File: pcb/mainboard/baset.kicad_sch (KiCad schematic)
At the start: 47 parts, among them U38 ISL24021IRT065Z-T7A‎, U39 ISL24021IRT065Z-T7A‎, U40 ISL24021IRT065Z-T7A‎, U41 ISL24021IRT065Z-T7A‎, U42 DACx0508_WQFN, U43 ISL24021IRT065Z-T7A‎, U44 ISL24021IRT065Z-T7A‎, U45 ISL24021IRT065Z-T7A‎, U46 ISL24021IRT065Z-T7A‎, U8 XC7K70T-2FBG484C

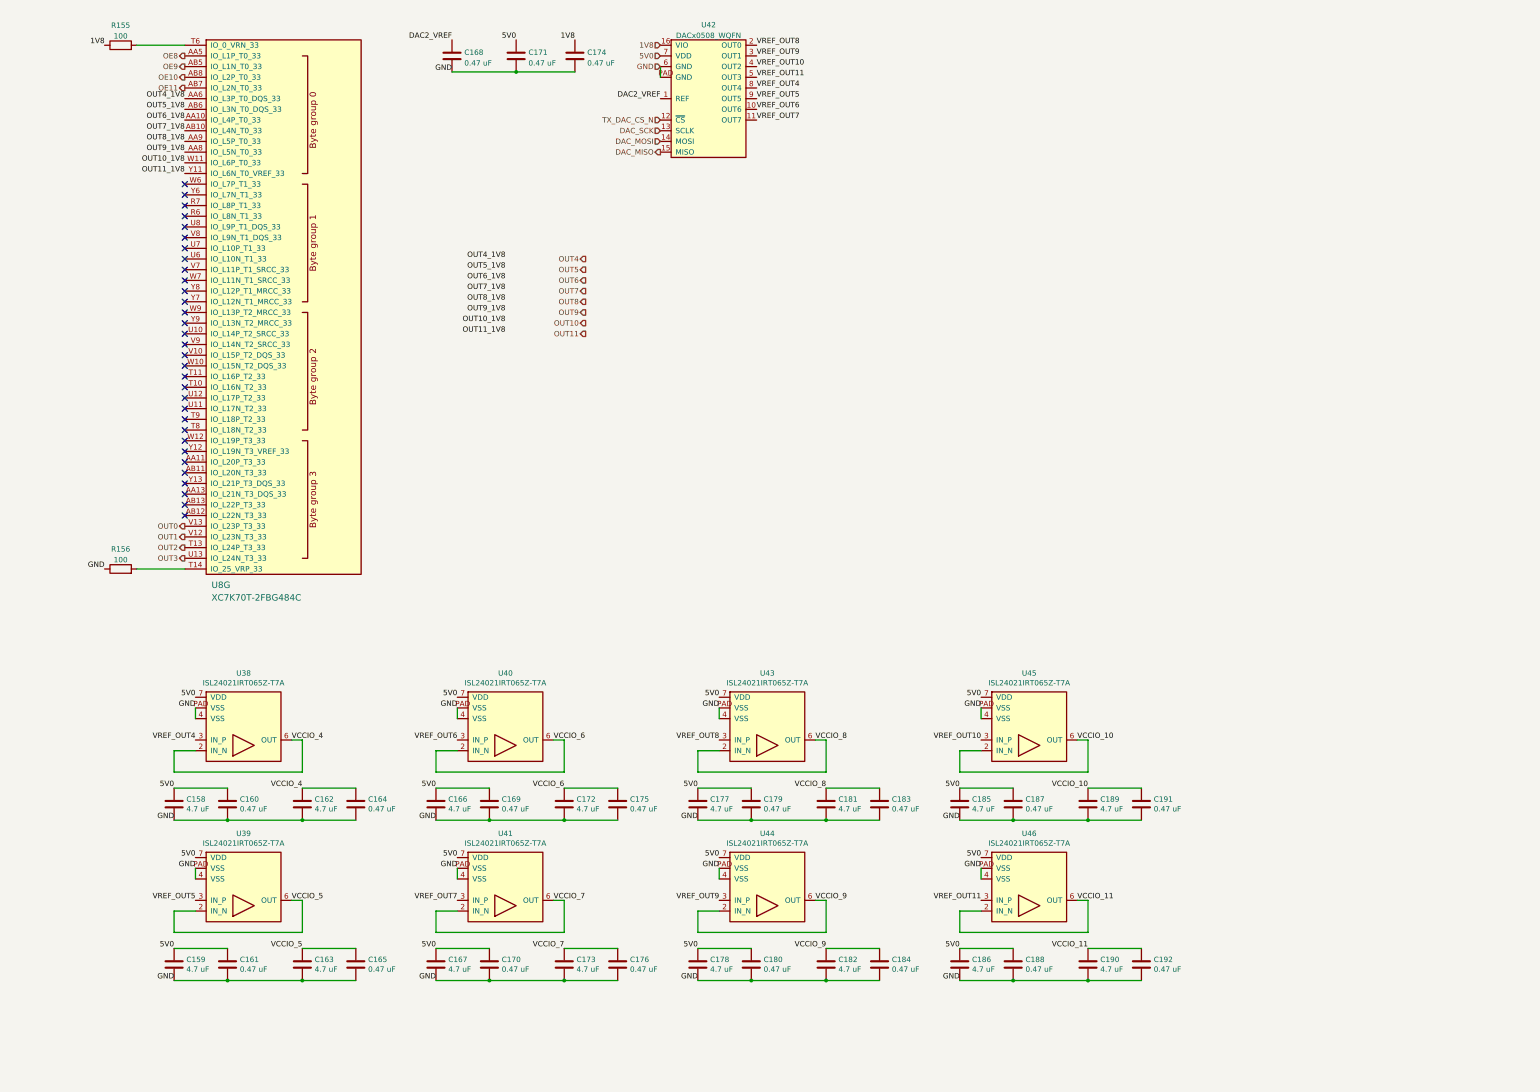
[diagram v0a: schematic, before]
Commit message: Continued initial work on main board
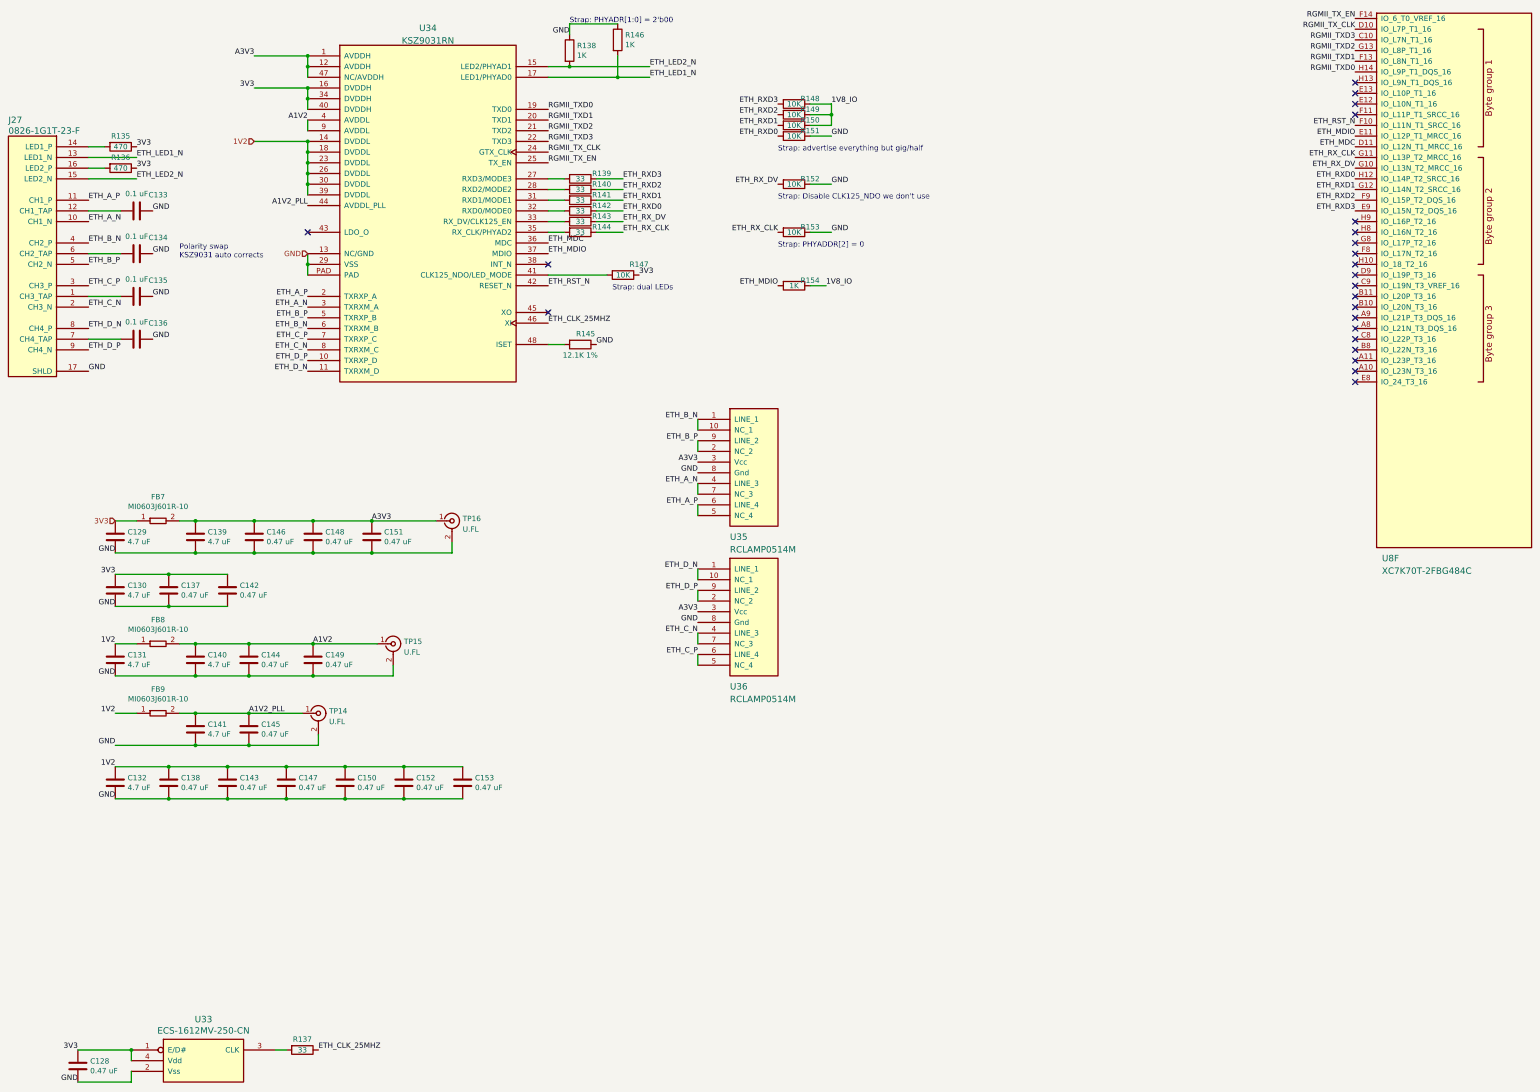
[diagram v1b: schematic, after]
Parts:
- removed C158, C159, C162, C163, C166, C167, C172, C173, C177, C178, C181, C182, C185, C186, C189, C190: 4.7 uF, azonenberg_pcb:EIA_0603_CAP_NOSILK, symbol device:C
- removed C160, C161, C164, C165, C169, C170, C175, C176, C179, C180, C183, C184, C187, C188, C191, C192: 0.47 uF, azonenberg_pcb:EIA_0402_CAP_NOSILK, symbol device:C
- removed C168, C171, C174: 0.47 uF, symbol device:C
- removed R155, R156: 100, symbol device:R
- removed U38, U39, U40, U41, U43, U44, U45, U46: ISL24021IRT065Z-T7A‎, azonenberg_pcb:DFN_8_0.65MM_3x3MM, symbol analog-azonenberg:ISL24021IRT065Z-T7A‎
- removed U42: DACx0508_WQFN, symbol analog-azonenberg:DACx0508_WQFN
- removed U8: XC7K70T-2FBG484C, symbol xilinx-azonenberg:XC7KxT-FBG484
- added C128, C137, C138, C142, C143, C144, C145, C146, C147, C148, C149, C150, C151, C152, C153: 0.47 uF, symbol device:C
- added C129, C130, C131, C132, C139, C140, C141: 4.7 uF, symbol device:C
- added C133, C134, C135, C136: 0.1 uF, symbol device:C
- added FB7, FB8, FB9: MI0603J601R-10, symbol passive-azonenberg:FERRITE_SMALL2
- added J27: 0826-1G1T-23-F, symbol special-azonenberg:BEL_FUSE_0826-1G1T-23-F
- added R135, R136: 470, symbol device:R
- added R137, R139, R140, R141, R142, R143, R144: 33, symbol device:R
- added R138, R146, R154: 1K, symbol device:R
- added R145: 12.1K 1%, symbol device:R
- added R147, R148, R149, R150, R151, R152, R153: 10K, symbol device:R
- added TP14, TP15, TP16: U.FL, symbol conn:CONN_COAXIAL
- added U33: ECS-1612MV-250-CN, symbol osc-azonenberg:OSC
- added U34: KSZ9031RN, symbol special-azonenberg:KSZ9031RN
- added U35, U36: RCLAMP0514M, symbol special-azonenberg:RCLAMP0514M
- added U8: XC7K70T-2FBG484C, symbol xilinx-azonenberg:XC7KxT-FBG484
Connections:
- net GND: now also C128.2, C129.2, C130.2, C131.2, C132.2, C133.1, C134.1, C135.1, C136.1, C137.2, C138.2, C139.2, C140.2, C141.2, C142.2, C143.2, C144.2, C145.2, C146.2, C147.2, C148.2, C149.2, C150.2, C151.2, C152.2, C153.2, J27.17 (SHLD), R138.1, R145.1, R146.1, R151.1, R152.1, R153.1, TP14.2 (Ext), TP15.2 (Ext), TP16.2 (Ext), U33.2 (Vss), U34.13 (NC/GND), U34.29 (VSS), U34.PAD, U35.8 (Gnd), U36.8 (Gnd)
- new net: R147.2, U34.41 (CLK125_NDO/LED_MODE)
- new net: R140.2, U34.28 (RXD2/MODE2)
- new net: R145.2, U34.48 (ISET)
- new net: C133.2, J27.12 (CH1_TAP)
- new net: R139.2, U34.27 (RXD3/MODE3)
- new net: C135.2, J27.1 (CH3_TAP)
- new net: J27.14 (LED1_P), R135.2
- new net: J27.16 (LED2_P), R136.2
- new net: C134.2, J27.6 (CH2_TAP)
- new net: C136.2, J27.7 (CH4_TAP)
- new net: R141.2, U34.31 (RXD1/MODE1)
- new net: R142.2, U34.32 (RXD0/MODE0)
- new net: R143.2, U34.33 (RX_DV/CLK125_EN)
- new net: R144.2, U34.35 (RX_CLK/PHYAD2)
- new net: R137.2, U33.3 (CLK)
- new net 1V2: C131.1, C132.1, C138.1, C143.1, C147.1, C150.1, C152.1, C153.1, FB8.1, FB9.1, U34.14 (DVDDL), U34.18 (DVDDL), U34.23 (DVDDL), U34.26 (DVDDL), U34.30 (DVDDL), U34.39 (DVDDL)
- new net 1V8_IO: R148.1, R149.1, R150.1, R154.1
- new net 3V3: C128.1, C129.1, C130.1, C137.1, C142.1, FB7.1, R135.1, R136.1, R147.1, U33.1 (E/D#), U33.4 (Vdd), U34.16 (DVDDH), U34.34 (DVDDH), U34.40 (DVDDH)
- new net A1V2: C140.1, C144.1, C149.1, FB8.2, TP15.1 (In), U34.4 (AVDDL), U34.9 (AVDDL)
- new net A1V2_PLL: C141.1, C145.1, FB9.2, TP14.1 (In), U34.44 (AVDDL_PLL)
- new net A3V3: C139.1, C146.1, C148.1, C151.1, FB7.2, TP16.1 (In), U34.1 (AVDDH), U34.12 (AVDDH), U34.47 (NC/AVDDH), U35.3 (Vcc), U36.3 (Vcc)
- new net ETH_A_N: J27.10 (CH1_N), U34.3 (TXRXM_A), U35.4 (LINE_3), U35.7 (NC_3)
- new net ETH_A_P: J27.11 (CH1_P), U34.2 (TXRXP_A), U35.5 (NC_4), U35.6 (LINE_4)
- new net ETH_B_N: J27.4 (CH2_P), U34.6 (TXRXM_B), U35.1 (LINE_1), U35.10 (NC_1)
- new net ETH_B_P: J27.5 (CH2_N), U34.5 (TXRXP_B), U35.2 (NC_2), U35.9 (LINE_2)
- new net ETH_CLK_25MHZ: R137.1, U34.46 (XI)
- new net ETH_C_N: J27.2 (CH3_N), U34.8 (TXRXM_C), U36.4 (LINE_3), U36.7 (NC_3)
- new net ETH_C_P: J27.3 (CH3_P), U34.7 (TXRXP_C), U36.5 (NC_4), U36.6 (LINE_4)
- new net ETH_D_N: J27.8 (CH4_P), U34.11 (TXRXM_D), U36.1 (LINE_1), U36.10 (NC_1)
- new net ETH_D_P: J27.9 (CH4_N), U34.10 (TXRXP_D), U36.2 (NC_2), U36.9 (LINE_2)
- new net ETH_LED1_N: J27.13 (LED1_N), R146.2, U34.17 (LED1/PHYAD0)
- new net ETH_LED2_N: J27.15 (LED2_N), R138.2, U34.15 (LED2/PHYAD1)
- new net ETH_MDC: U34.36 (MDC), U8.D11 (IO_L12N_T1_MRCC_16)
- new net ETH_MDIO: R154.2, U34.37 (MDIO), U8.E11 (IO_L12P_T1_MRCC_16)
- new net ETH_RST_N: U34.42 (RESET_N), U8.F10 (IO_L11N_T1_SRCC_16)
- new net ETH_RXD0: R142.1, R151.2, U8.H12 (IO_L14P_T2_SRCC_16)
- new net ETH_RXD1: R141.1, R150.2, U8.G12 (IO_L14N_T2_SRCC_16)
- new net ETH_RXD2: R140.1, R149.2, U8.F9 (IO_L15P_T2_DQS_16)
- new net ETH_RXD3: R139.1, R148.2, U8.E9 (IO_L15N_T2_DQS_16)
- new net ETH_RX_CLK: R144.1, R153.2, U8.G11 (IO_L13P_T2_MRCC_16)
- new net ETH_RX_DV: R143.1, R152.2, U8.G10 (IO_L13N_T2_MRCC_16)
- new net RGMII_TXD0: U34.19 (TXD0), U8.H14 (IO_L9P_T1_DQS_16)
- new net RGMII_TXD1: U34.20 (TXD1), U8.F13 (IO_L8N_T1_16)
- new net RGMII_TXD2: U34.21 (TXD2), U8.G13 (IO_L8P_T1_16)
- new net RGMII_TXD3: U34.22 (TXD3), U8.C10 (IO_L7N_T1_16)
- new net RGMII_TX_CLK: U34.24 (GTX_CLK), U8.D10 (IO_L7P_T1_16)
- new net RGMII_TX_EN: U34.25 (TX_EN), U8.F14 (IO_6_T0_VREF_16)
- no-connect marks 32 -> 23
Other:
- note added: "Polarity swap KSZ9031 auto corrects"
- note added: "Strap: Disable CLK125_NDO we don't use"
- note added: "Strap: PHYADDR[2] = 0"
- note added: "Strap: PHYADR[1:0] = 2'b00"
- note added: "Strap: advertise everything but gig/half"
- note added: "Strap: dual LEDs"

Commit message: Calculated power monitor voltage divider
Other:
- company: (none) -> Antikernel Labs
- title: (none) -> Trigger Crossbar
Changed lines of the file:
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@@
 (kicad_sch (version 20211123) (generator eeschema)
   (paper "A3")
+  (title_block
+    (title "Trigger Crossbar")
+    (date "2023-12-17")
+    (rev "0.1")
+    (company "Antikernel Labs")
+    (comment 1 "Andrew D. Zonenberg")
+  )
   (junction (at 121.92 198.12) (diameter 0) (color 0 0 0 0)
   )

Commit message: Began assigning footprints
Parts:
- C128, C133, C134, C135, C136, C137, C138, C142, C143, C144, C145, C146, C147, C148, C149, C150, C151, C152, C153: footprint (none) -> azonenberg_pcb:EIA_0402_CAP_NOSILK
- C129, C130, C131, C132, C139, C140, C141: footprint (none) -> azonenberg_pcb:EIA_0603_CAP_NOSILK
- FB7, FB8, FB9: footprint (none) -> azonenberg_pcb:EIA_0603_INDUCTOR_NOSILK
- J27: footprint (none) -> azonenberg_pcb:CONN_BELFUSE_0826_1G1T_23_F
- R135, R136, R137, R138, R139, R140, R141, R142, R143, R144, R145, R146, R147, R148, R149, R150, R151, R152, R153, R154: footprint (none) -> azonenberg_pcb:EIA_0402_RES_NOSILK
- TP14, TP15, TP16: footprint (none) -> azonenberg_pcb:CONN_U.FL_TE_1909763-1
- U34: footprint (none) -> azonenberg_pcb:QFN_48_0.5MM_7x7MM
- U35, U36: footprint (none) -> azonenberg_pcb:SOP_10_0.5MM_3MM
- U8: footprint (none) -> azonenberg_pcb:BGA_484_22x22_FULLARRAY_1MM

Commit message: Finished component footprint assignment, started some EM simulations. Ready for schematic review.
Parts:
- U33: footprint (none) -> azonenberg_pcb:OSCILLATOR_1.6x1.2
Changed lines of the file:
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@@
   (title_block
     (title "Trigger Crossbar")
-    (date "2023-12-17")
+    (date "2023-12-18")
     (rev "0.1")
     (company "Antikernel Labs")
@@
       (effects (font (size 1.524 1.524)))
     )
-    (property "Footprint" "" (id 2) (at 74.93 265.43 0)
+    (property "Footprint" "azonenberg_pcb:OSCILLATOR_1.6x1.2" (id 2) (at 74.93 265.43 0)
       (effects (font (size 1.524 1.524)) hide)
     )

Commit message: Finished initial schematic review of trigger crossbar mainboard
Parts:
- added C236, C237: 4.7 uF, azonenberg_pcb:EIA_0603_CAP_NOSILK, symbol device:C
- added FB10: MI0603J601R-10, azonenberg_pcb:EIA_0603_INDUCTOR_NOSILK, symbol passive-azonenberg:FERRITE_SMALL2
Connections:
- net 1V2: now also C236.1, FB10.1; no longer C132.1, C138.1, C143.1, C147.1, C150.1, C152.1, C153.1, U34.14 (DVDDL), U34.18 (DVDDL), U34.23 (DVDDL), U34.26 (DVDDL), U34.30 (DVDDL), U34.39 (DVDDL)
- net GND: now also C236.2, C237.2
- new net D1V2: C132.1, C138.1, C143.1, C147.1, C150.1, C152.1, C153.1, C237.1, FB10.2, U34.14 (DVDDL), U34.18 (DVDDL), U34.23 (DVDDL), U34.26 (DVDDL), U34.30 (DVDDL), U34.39 (DVDDL)
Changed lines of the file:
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@@
   (title_block
     (title "Trigger Crossbar")
-    (date "2023-12-18")
+    (date "2023-12-19")
     (rev "0.1")
     (company "Antikernel Labs")
@@
     (stroke (width 0) (type default) (color 0 0 0 0))
   )
+  (wire (pts (xy 53.34 130.81) (xy 68.58 130.81))
+    (stroke (width 0) (type default) (color 0 0 0 0))
+  )
   (wire (pts (xy 72.39 147.32) (xy 86.36 147.32))
     (stroke (width 0) (type default) (color 0 0 0 0))
@@
     (stroke (width 0) (type default) (color 0 0 0 0))
   )
+  (wire (pts (xy 53.34 123.19) (xy 58.42 123.19))
+    (stroke (width 0) (type default) (color 0 0 0 0))
+  )
   (wire (pts (xy 99.06 36.83) (xy 99.06 39.37))
     (stroke (width 0) (type default) (color 0 0 0 0))
@@
     (effects (font (size 1.27 1.27)) (justify left bottom))
   )
+  (label "D1V2" (at 86.36 49.53 180)
+    (effects (font (size 1.27 1.27)) (justify right bottom))
+  )
   (label "RGMII_TX_CLK" (at 156.21 52.07 0)
     (effects (font (size 1.27 1.27)) (justify left bottom))
@@
     (effects (font (size 1.27 1.27)) (justify left bottom))
   )
-  (label "1V2" (at 53.34 198.12 180)
+  (label "D1V2" (at 53.34 198.12 180)
     (effects (font (size 1.27 1.27)) (justify right bottom))
   )
@@
     (effects (font (size 1.27 1.27)) (justify right bottom))
   )
+  (label "D1V2" (at 68.58 123.19 0)
+    (effects (font (size 1.27 1.27)) (justify left bottom))
+  )
   (label "ETH_MDIO" (at 347.98 48.26 180)
     (effects (font (size 1.27 1.27)) (justify right bottom))
@@
   )
   (label "ETH_RX_DV" (at 210.82 59.69 180)
+    (effects (font (size 1.27 1.27)) (justify right bottom))
+  )
+  (label "GND" (at 53.34 130.81 180)
     (effects (font (size 1.27 1.27)) (justify right bottom))
   )
@@
     (effects (font (size 1.27 1.27)) (justify right))
   )
-  (hierarchical_label "1V2" (shape input) (at 86.36 49.53 180)
+  (hierarchical_label "1V2" (shape input) (at 53.34 123.19 180)
     (effects (font (size 1.27 1.27)) (justify right))
   )
@@
     (property "Datasheet" "" (id 3) (at 58.42 66.04 0)
       (effects (font (size 1.27 1.27)) hide)
+    )
+    (pin "1")
+    (pin "2")
+  )
+  (symbol (lib_id "passive-azonenberg:FERRITE_SMALL2") (at 63.5 123.19 0) (unit 1)
+    (in_bom yes) (on_board yes)
+    (property "Reference" "FB10" (id 0) (at 63.5 117.475 0))
+    (property "Value" "MI0603J601R-10" (id 1) (at 63.5 119.7864 0))
+    (property "Footprint" "azonenberg_pcb:EIA_0603_INDUCTOR_NOSILK" (id 2) (at 63.5 123.19 0)
+      (effects (font (size 1.524 1.524)) hide)
+    )
+    (property "Datasheet" "" (id 3) (at 63.5 123.19 0)
+      (effects (font (size 1.524 1.524)))
     )
     (pin "1")
@@
     )
     (property "Datasheet" "" (id 3) (at 58.42 96.52 0)
+      (effects (font (size 1.27 1.27)) hide)
+    )
+    (pin "1")
+    (pin "2")
+  )
+  (symbol (lib_id "device:C") (at 53.34 127 0) (unit 1)
+    (in_bom yes) (on_board yes)
+    (property "Reference" "C236" (id 0) (at 56.261 125.8316 0)
+      (effects (font (size 1.27 1.27)) (justify left))
+    )
+    (property "Value" "4.7 uF" (id 1) (at 56.261 128.143 0)
+      (effects (font (size 1.27 1.27)) (justify left))
+    )
+    (property "Footprint" "azonenberg_pcb:EIA_0603_CAP_NOSILK" (id 2) (at 54.3052 130.81 0)
+      (effects (font (size 1.27 1.27)) hide)
+    )
+    (property "Datasheet" "" (id 3) (at 53.34 127 0)
       (effects (font (size 1.27 1.27)) hide)
     )
@@
     (pin "4")
   )
+  (symbol (lib_id "device:C") (at 68.58 127 0) (unit 1)
+    (in_bom yes) (on_board yes)
+    (property "Reference" "C237" (id 0) (at 71.501 125.8316 0)
+      (effects (font (size 1.27 1.27)) (justify left))
+    )
+    (property "Value" "4.7 uF" (id 1) (at 71.501 128.143 0)
+      (effects (font (size 1.27 1.27)) (justify left))
+    )
+    (property "Footprint" "azonenberg_pcb:EIA_0603_CAP_NOSILK" (id 2) (at 69.5452 130.81 0)
+      (effects (font (size 1.27 1.27)) hide)
+    )
+    (property "Datasheet" "" (id 3) (at 68.58 127 0)
+      (effects (font (size 1.27 1.27)) hide)
+    )
+    (pin "1")
+    (pin "2")
+  )
   (symbol (lib_id "device:R") (at 214.63 59.69 270) (unit 1)

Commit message: Continued initial layout work
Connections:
- net 1V8_IO is gone; now on net 3V3: R148.1, R149.1, R150.1, R154.1
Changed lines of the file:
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@@
   (title_block
     (title "Trigger Crossbar")
-    (date "2023-12-19")
+    (date "2023-12-20")
     (rev "0.1")
     (company "Antikernel Labs")
@@
     (effects (font (size 1.27 1.27)) (justify right bottom))
   )
-  (label "1V8_IO" (at 222.25 83.82 0)
+  (label "3V3" (at 222.25 83.82 0)
     (effects (font (size 1.27 1.27)) (justify left bottom))
   )
@@
     (effects (font (size 1.27 1.27)) (justify right bottom))
   )
-  (label "1V8_IO" (at 223.52 40.64 0)
-    (effects (font (size 1.27 1.27)) (justify left bottom))
-  )
+  (label "3V3" (at 223.52 40.64 0)
+    (effects (font (size 1.27 1.27)) (justify left bottom))
+  )
